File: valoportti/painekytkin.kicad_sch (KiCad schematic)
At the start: 12 parts, among them Q1 BC547, Q2 BC547, Q3 BC547

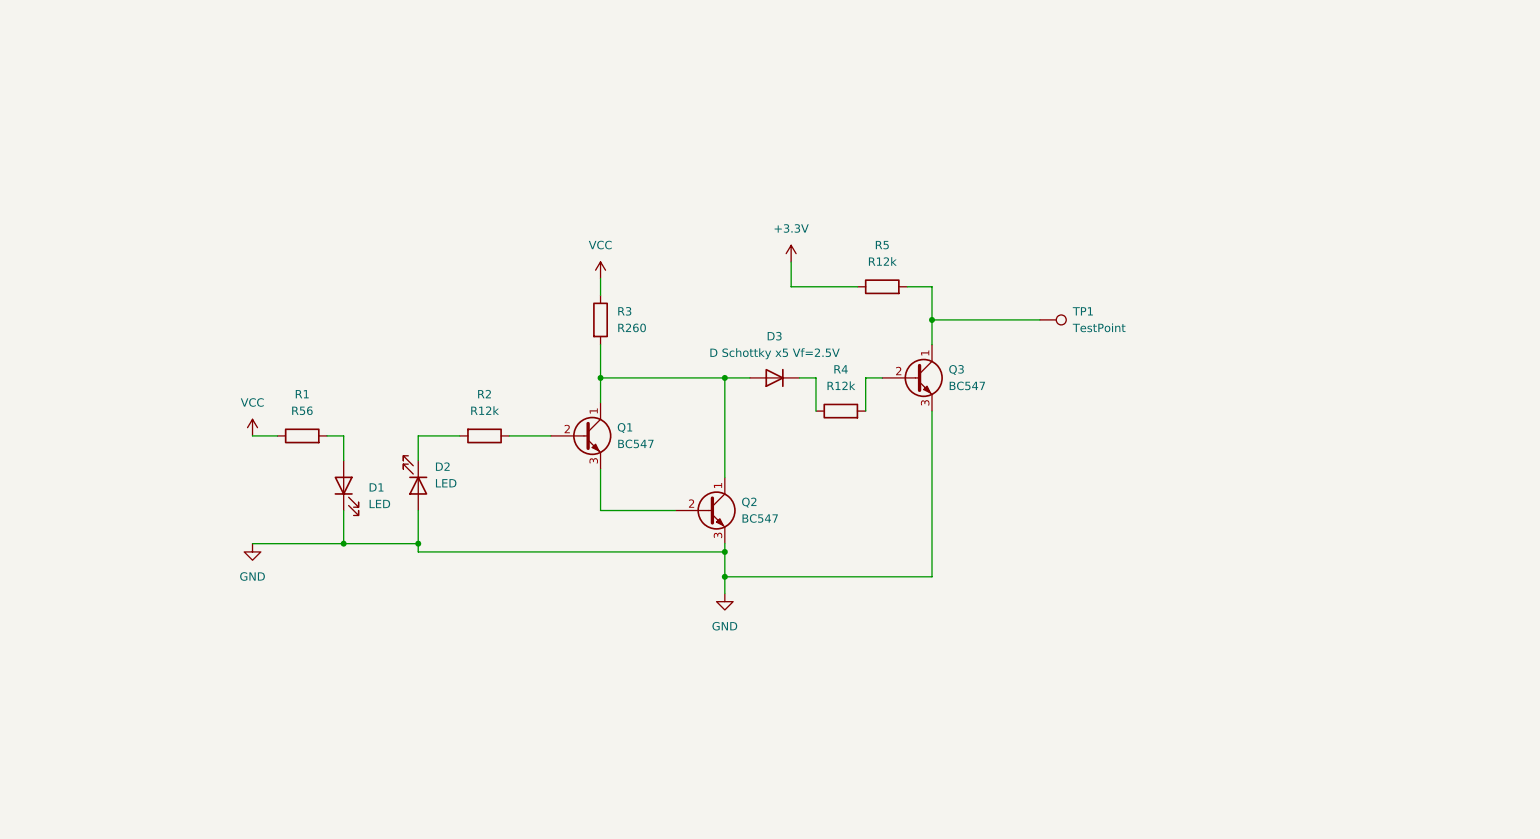
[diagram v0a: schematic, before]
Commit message: add simplified coupling to GPIO pin
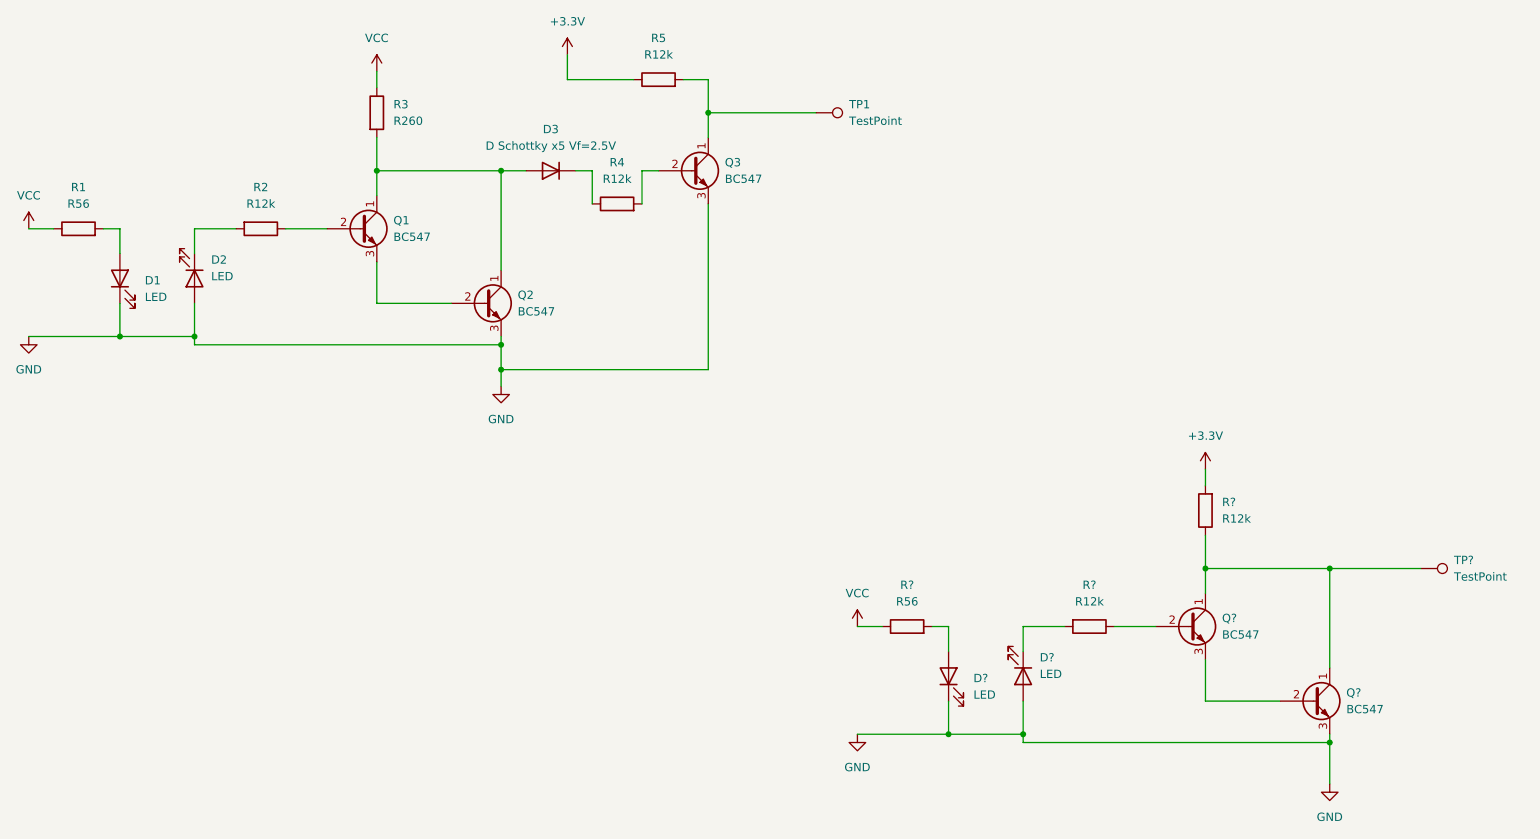
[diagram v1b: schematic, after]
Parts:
- added D? (x2): LED, symbol Device:LED
- added Q? (x2): BC547, Package_TO_SOT_THT:TO-92_Inline, symbol Transistor_BJT:BC547
- added R? (x2): R12k, symbol Device:R
- added R?: R56, symbol Device:R
- added TP?: TestPoint, symbol Connector:TestPoint
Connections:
- net +3V3: now also R?.2
- net GND: now also D?.1 (K), D?.2 (A), Q?.3 (E)
- net VCC: now also R?.1
- new net: Q?.1 (C), Q?.1 (C), R?.1, TP?.1
- new net: D?.2 (A), R?.2
- new net: Q?.2 (B), R?.1
- new net: Q?.2 (B), Q?.3 (E)
- new net: D?.1 (K), R?.2
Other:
- moved on the sheet: D1, D2, D3, Q1, Q2, Q3, R1, R2, R3, R4, R5, TP1

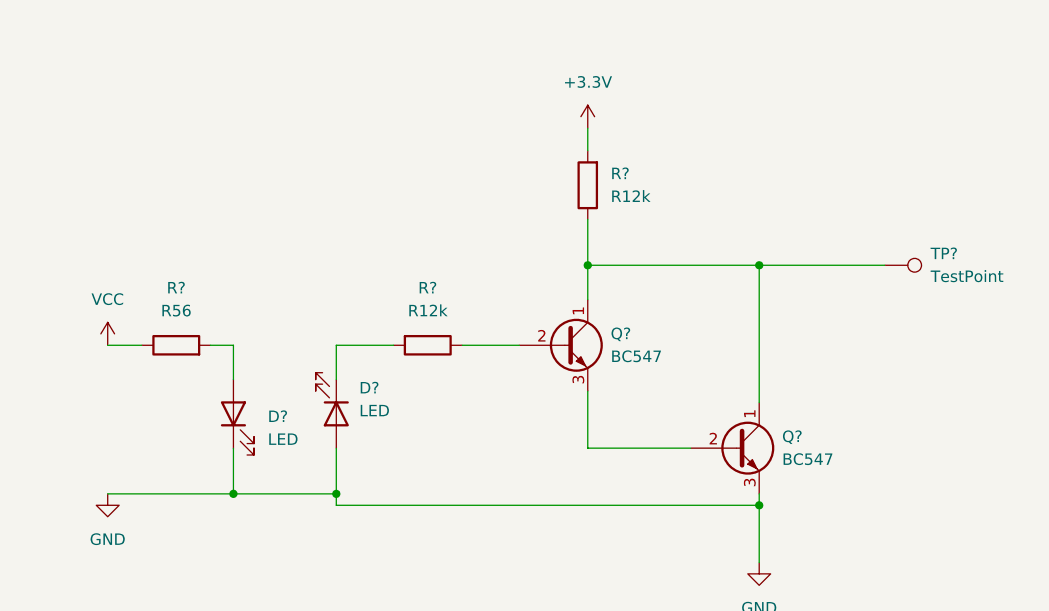
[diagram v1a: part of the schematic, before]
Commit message: add simplifier schematic annotations
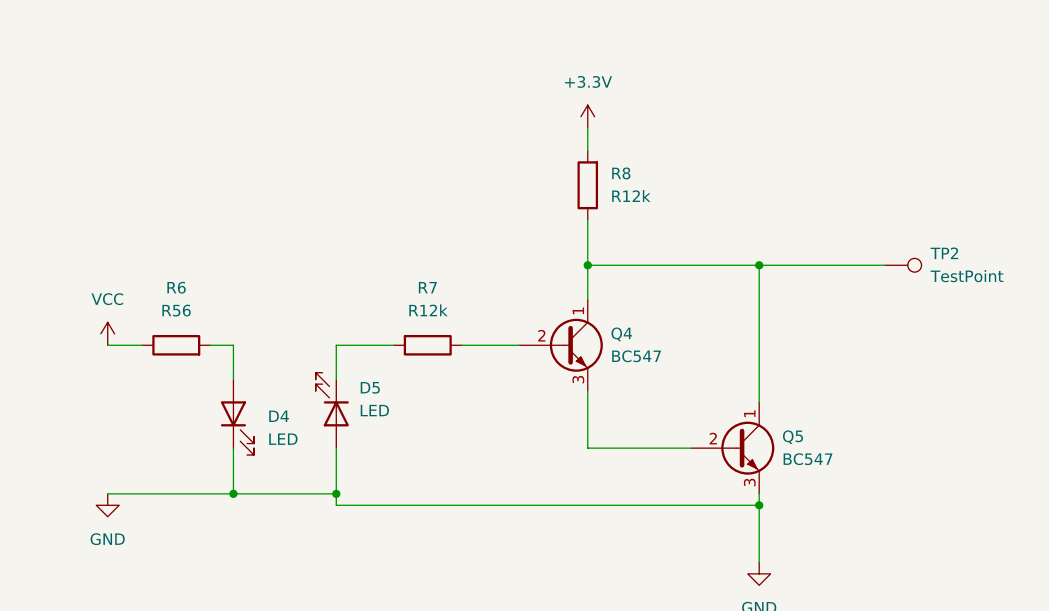
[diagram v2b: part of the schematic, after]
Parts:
- gave numbers to parts that had none: 8
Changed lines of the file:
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@@
   (symbol (lib_id "power:GND") (at 233.68 139.7 0) (unit 1)
     (in_bom yes) (on_board yes) (fields_autoplaced)
-    (property "Reference" "#PWR?" (id 0) (at 233.68 146.05 0)
+    (property "Reference" "#PWR05" (id 0) (at 233.68 146.05 0)
       (effects (font (size 1.27 1.27)) hide)
     )
@@
   (symbol (lib_id "Connector:TestPoint") (at 247.65 106.68 270) (unit 1)
     (in_bom yes) (on_board yes) (fields_autoplaced)
-    (property "Reference" "TP?" (id 0) (at 252.73 105.4099 90)
+    (property "Reference" "TP2" (id 0) (at 252.73 105.4099 90)
       (effects (font (size 1.27 1.27)) (justify left))
     )
@@
   (symbol (lib_id "Device:LED") (at 175.26 123.19 90) (unit 1)
     (in_bom yes) (on_board yes) (fields_autoplaced)
-    (property "Reference" "D?" (id 0) (at 179.07 123.5074 90)
+    (property "Reference" "D4" (id 0) (at 179.07 123.5074 90)
       (effects (font (size 1.27 1.27)) (justify right))
     )
@@
   (symbol (lib_id "Transistor_BJT:BC547") (at 212.09 115.57 0) (unit 1)
     (in_bom yes) (on_board yes) (fields_autoplaced)
-    (property "Reference" "Q?" (id 0) (at 217.17 114.2999 0)
+    (property "Reference" "Q4" (id 0) (at 217.17 114.2999 0)
       (effects (font (size 1.27 1.27)) (justify left))
     )
@@
   (symbol (lib_id "Device:LED") (at 186.69 123.19 270) (unit 1)
     (in_bom yes) (on_board yes) (fields_autoplaced)
-    (property "Reference" "D?" (id 0) (at 189.23 120.3324 90)
+    (property "Reference" "D5" (id 0) (at 189.23 120.3324 90)
       (effects (font (size 1.27 1.27)) (justify left))
     )
@@
   (symbol (lib_id "power:+3.3V") (at 214.63 91.44 0) (unit 1)
     (in_bom yes) (on_board yes) (fields_autoplaced)
-    (property "Reference" "#PWR?" (id 0) (at 214.63 95.25 0)
+    (property "Reference" "#PWR04" (id 0) (at 214.63 95.25 0)
       (effects (font (size 1.27 1.27)) hide)
     )
@@
   (symbol (lib_id "Device:R") (at 196.85 115.57 270) (unit 1)
     (in_bom yes) (on_board yes) (fields_autoplaced)
-    (property "Reference" "R?" (id 0) (at 196.85 109.22 90))
+    (property "Reference" "R7" (id 0) (at 196.85 109.22 90))
     (property "Value" "R12k" (id 1) (at 196.85 111.76 90))
     (property "Footprint" "" (id 2) (at 196.85 113.792 90)
@@
   (symbol (lib_id "Device:R") (at 168.91 115.57 90) (unit 1)
     (in_bom yes) (on_board yes) (fields_autoplaced)
-    (property "Reference" "R?" (id 0) (at 168.91 109.22 90))
+    (property "Reference" "R6" (id 0) (at 168.91 109.22 90))
     (property "Value" "R56" (id 1) (at 168.91 111.76 90))
     (property "Footprint" "" (id 2) (at 168.91 117.348 90)
@@
   (symbol (lib_id "power:GND") (at 161.29 132.08 0) (unit 1)
     (in_bom yes) (on_board yes) (fields_autoplaced)
-    (property "Reference" "#PWR?" (id 0) (at 161.29 138.43 0)
+    (property "Reference" "#PWR03" (id 0) (at 161.29 138.43 0)
       (effects (font (size 1.27 1.27)) hide)
     )
@@
   (symbol (lib_id "power:+3.3V") (at 116.84 27.94 0) (unit 1)
     (in_bom yes) (on_board yes) (fields_autoplaced)
-    (property "Reference" "#PWR?" (id 0) (at 116.84 31.75 0)
+    (property "Reference" "#PWR01" (id 0) (at 116.84 31.75 0)
       (effects (font (size 1.27 1.27)) hide)
     )
@@
   (symbol (lib_id "power:VCC") (at 161.29 115.57 0) (unit 1)
     (in_bom yes) (on_board yes) (fields_autoplaced)
-    (property "Reference" "#PWR?" (id 0) (at 161.29 119.38 0)
+    (property "Reference" "#PWR02" (id 0) (at 161.29 119.38 0)
       (effects (font (size 1.27 1.27)) hide)
     )
@@
   (symbol (lib_id "Transistor_BJT:BC547") (at 231.14 127 0) (unit 1)
     (in_bom yes) (on_board yes) (fields_autoplaced)
-    (property "Reference" "Q?" (id 0) (at 236.22 125.7299 0)
+    (property "Reference" "Q5" (id 0) (at 236.22 125.7299 0)
       (effects (font (size 1.27 1.27)) (justify left))
     )
@@
   (symbol (lib_id "Device:R") (at 214.63 97.79 180) (unit 1)
     (in_bom yes) (on_board yes) (fields_autoplaced)
-    (property "Reference" "R?" (id 0) (at 217.17 96.5199 0)
+    (property "Reference" "R8" (id 0) (at 217.17 96.5199 0)
       (effects (font (size 1.27 1.27)) (justify right))
     )
@@
   )
   (symbol_instances
+    (path "/89aaad01-246b-44f3-81f6-c3fa90274c74"
+      (reference "#PWR01") (unit 1) (value "+3.3V") (footprint "")
+    )
+    (path "/d3a83e03-332b-4204-a382-59c990440b63"
+      (reference "#PWR02") (unit 1) (value "VCC") (footprint "")
+    )
+    (path "/86fc3bd4-8f9e-4006-8a25-85c1a75dc525"
+      (reference "#PWR03") (unit 1) (value "GND") (footprint "")
+    )
+    (path "/5260fcac-ebfd-4aa8-991f-972aba159a61"
+      (reference "#PWR04") (unit 1) (value "+3.3V") (footprint "")
+    )
+    (path "/1bed61ce-b97f-4149-add4-961c945fd1bc"
+      (reference "#PWR05") (unit 1) (value "GND") (footprint "")
+    )
     (path "/2710818b-9b7a-42f1-b4a4-5012463263a7"
       (reference "#PWR0101") (unit 1) (value "GND") (footprint "")
@@
       (reference "#PWR0104") (unit 1) (value "VCC") (footprint "")
     )
-    (path "/1bed61ce-b97f-4149-add4-961c945fd1bc"
-      (reference "#PWR?") (unit 1) (value "GND") (footprint "")
-    )
-    (path "/5260fcac-ebfd-4aa8-991f-972aba159a61"
-      (reference "#PWR?") (unit 1) (value "+3.3V") (footprint "")
-    )
-    (path "/86fc3bd4-8f9e-4006-8a25-85c1a75dc525"
-      (reference "#PWR?") (unit 1) (value "GND") (footprint "")
-    )
-    (path "/89aaad01-246b-44f3-81f6-c3fa90274c74"
-      (reference "#PWR?") (unit 1) (value "+3.3V") (footprint "")
-    )
-    (path "/d3a83e03-332b-4204-a382-59c990440b63"
-      (reference "#PWR?") (unit 1) (value "VCC") (footprint "")
-    )
     (path "/5c378429-9b24-44a9-8c23-a863241e2750"
       (reference "D1") (unit 1) (value "LED") (footprint "")
@@
     )
     (path "/3b4c917c-52d5-462c-95c1-773cbc93a2b6"
-      (reference "D?") (unit 1) (value "LED") (footprint "")
+      (reference "D4") (unit 1) (value "LED") (footprint "")
     )
     (path "/51e34bb6-0d12-41f5-b330-2b1032aedf7a"
-      (reference "D?") (unit 1) (value "LED") (footprint "")
+      (reference "D5") (unit 1) (value "LED") (footprint "")
     )
     (path "/4654e364-134c-4319-9ec8-84995283aaa2"
@@
     )
     (path "/3deedf83-48a4-4c7f-a205-07f645d1a6c4"
-      (reference "Q?") (unit 1) (value "BC547") (footprint "Package_TO_SOT_THT:TO-92_Inline")
+      (reference "Q4") (unit 1) (value "BC547") (footprint "Package_TO_SOT_THT:TO-92_Inline")
     )
     (path "/dc869806-fad8-4cf9-9dc4-027d29f1157b"
-      (reference "Q?") (unit 1) (value "BC547") (footprint "Package_TO_SOT_THT:TO-92_Inline")
+      (reference "Q5") (unit 1) (value "BC547") (footprint "Package_TO_SOT_THT:TO-92_Inline")
     )
     (path "/b58e92e1-ab7e-4195-b00a-13e80508d8b6"
@@
       (reference "R5") (unit 1) (value "R12k") (footprint "")
     )
+    (path "/79ed84ec-da69-42cc-8bf0-865adb4cb48b"
+      (reference "R6") (unit 1) (value "R56") (footprint "")
+    )
     (path "/5e8a4e0a-64ca-4013-a037-ae6218497a1b"
-      (reference "R?") (unit 1) (value "R12k") (footprint "")
-    )
-    (path "/79ed84ec-da69-42cc-8bf0-865adb4cb48b"
-      (reference "R?") (unit 1) (value "R56") (footprint "")
+      (reference "R7") (unit 1) (value "R12k") (footprint "")
     )
     (path "/fe683913-4029-4e7b-889f-3763693d3316"
-      (reference "R?") (unit 1) (value "R12k") (footprint "")
+      (reference "R8") (unit 1) (value "R12k") (footprint "")
     )
     (path "/0ae3d527-0f2e-4f13-b015-a629a93d7ccd"
@@
     )
     (path "/3845f39a-1325-4724-a5c7-74584df9f70c"
-      (reference "TP?") (unit 1) (value "TestPoint") (footprint "")
-    )
-  )
+      (reference "TP2") (unit 1) (value "TestPoint") (footprint "")
+    )
+  )
